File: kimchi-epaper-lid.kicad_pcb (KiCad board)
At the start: 4 copper layers, 65 x 32 mm, 8 parts, among them J1 DF40HC(3.5)-60DS, J2 DF40HC(3.5)-60DS, U1 24C32

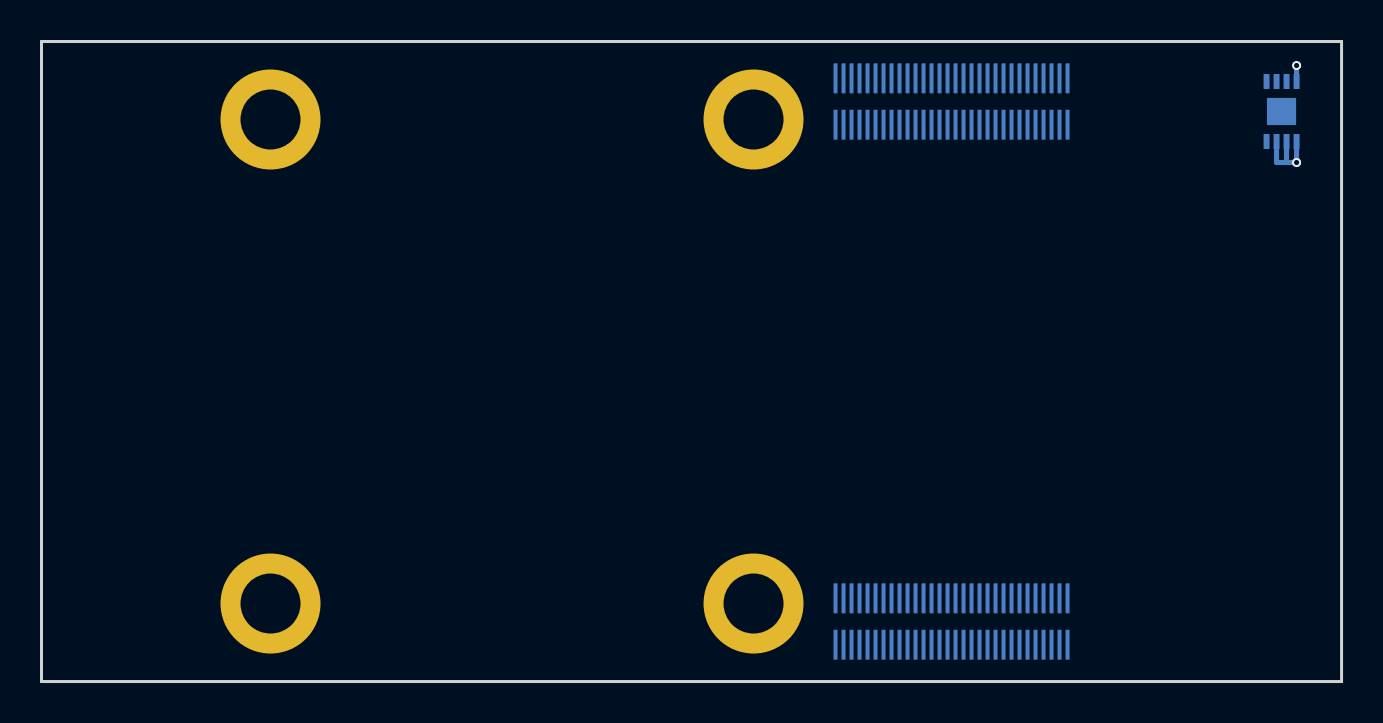
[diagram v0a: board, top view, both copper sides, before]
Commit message: prouting a few components and updated position
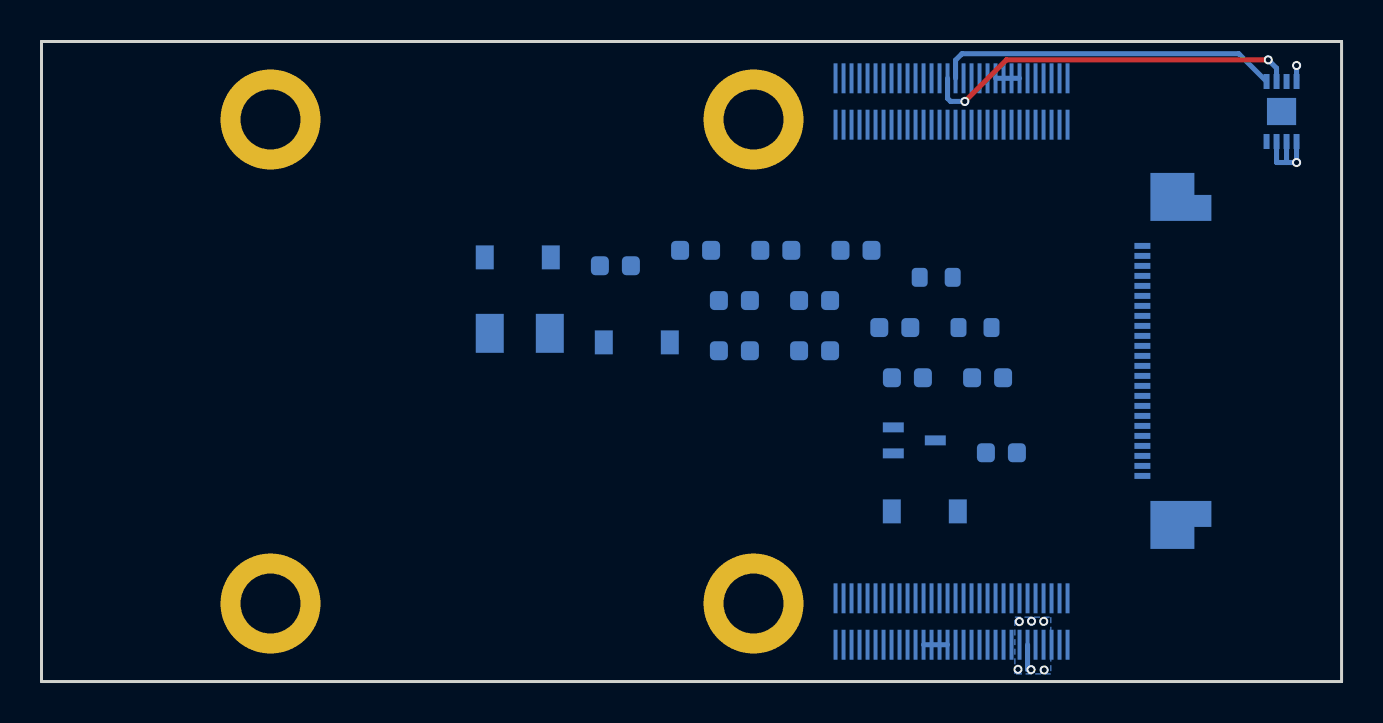
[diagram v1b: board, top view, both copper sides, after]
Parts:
- added C1: 2.2uF, Capacitor_SMD:C_0603_1608Metric, B.Cu at (154.3, 110.8)
- added C10: 1uF, Capacitor_SMD:C_0603_1608Metric, B.Cu at (149.7, 108.3)
- added C11: 1uF, Capacitor_SMD:C_0603_1608Metric, B.Cu at (141.6, 109.5)
- added C12: 0.1uF, Capacitor_SMD:C_0603_1608Metric, B.Cu at (147.7, 104.4)
- added C2: 1uF, Capacitor_SMD:C_0603_1608Metric, B.Cu at (135.7, 105.2)
- added C3: 1uF, Capacitor_SMD:C_0603_1608Metric, B.Cu at (145.7, 109.5)
- added C4: 1uF, Capacitor_SMD:C_0603_1608Metric, B.Cu at (141.6, 107.0)
- added C5: 1uF, Capacitor_SMD:C_0603_1608Metric, B.Cu at (139.7, 104.4)
- added C6: 1uF, Capacitor_SMD:C_0603_1608Metric, B.Cu at (150.3, 110.8)
- added C7: 1uF, Capacitor_SMD:C_0603_1608Metric, B.Cu at (143.7, 104.4)
- added C8: 1uF, Capacitor_SMD:C_0603_1608Metric, B.Cu at (145.7, 107.0)
- added C9: 1uF, Capacitor_SMD:C_0603_1608Metric, B.Cu at (155.0, 114.6)
- added D1: MBR0530T3G, Diode_SMD:D_SOD-123, B.Cu at (130.8, 104.8)
- added D2: MBR0530T3G, Diode_SMD:D_SOD-123, B.Cu at (136.8, 109.0)
- added D3: MBR0530T3G, Diode_SMD:D_SOD-123, B.Cu at (151.2, 117.5)
- added L1: 68uH, NLV32T-680J-EF:INDM3225X240N, B.Cu at (130.9, 108.6)
- added Q1: SI1308EDL-T1-BE3, SI1308EDL-T1-BE3:SOT65P210X110-3N, B.Cu at (150.6, 113.9)
- added R1: 10k, Resistor_SMD:R_0603_1608Metric, B.Cu at (153.7, 108.3)
- added R2: 2.2k, Resistor_SMD:R_0603_1608Metric, B.Cu at (151.7, 105.8)
- added X1: 52435-2471, epaper-fpc-connector:MOLEX_52435-2471, B.Cu at (162.0, 110.0)
- renumbered H3 to H2, H2 to H3
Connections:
- J1 pad 1: (no net) -> /USDHC3_CMD
- J1 pad 17: (no net) -> I2C3_SDA
- J1 pad 18: (no net) -> I2C3_SCL
- J1 pad 19: (no net) -> I2C2_SDA
- J1 pad 2: (no net) -> /USDHC3_CLK
- J1 pad 20: (no net) -> I2C2_SCL
- J1 pad 21: (no net) -> I2C1_SDA
- J1 pad 22: (no net) -> I2C1_SCL
- J1 pad 23: (no net) -> ECSPI1_SCLK
- J1 pad 24: (no net) -> ECSPI1_SS0
- J1 pad 25: (no net) -> ECSPI1_MOSI
- J1 pad 26: (no net) -> ECSPI1_MISO
- J1 pad 27: (no net) -> ECSPI2_SCLK
- J1 pad 28: (no net) -> ECSPI2_SS0
- J1 pad 29: (no net) -> ECSPI2_MOSI
- J1 pad 3: (no net) -> /USDHC3_DATA3
- J1 pad 30: (no net) -> ECSPI2_MISO
- J1 pad 31: (no net) -> /DISP_D0_N
- J1 pad 32: (no net) -> /DISP_D0_P
- J1 pad 33: (no net) -> /DISP_D1_N
- J1 pad 34: (no net) -> /DISP_D1_P
- J1 pad 35: (no net) -> /DISP_CK_N
- J1 pad 36: (no net) -> /DISP_CK_P
- J1 pad 37: (no net) -> /DISP_D2_N
- J1 pad 38: (no net) -> /DISP_D2_P
- J1 pad 39: (no net) -> /DISP_D3_N
- J1 pad 4: (no net) -> /USDHC3_DATA0
- J1 pad 40: (no net) -> /DISP_D3_P
- J1 pad 41: (no net) -> /CAM_D0_N
- J1 pad 42: (no net) -> /CAM_D0_P
- J1 pad 43: (no net) -> /CAM_D1_N
- J1 pad 44: (no net) -> /CAM_D1_P
- J1 pad 45: (no net) -> /CAM_CK_N
- J1 pad 46: (no net) -> /CAM_CK_P
- J1 pad 47: (no net) -> /CAM_D2_N
- J1 pad 48: (no net) -> /CAM_D2_P
- J1 pad 49: (no net) -> /CAM_D3_N
- J1 pad 5: (no net) -> /USDHC3_DATA1
- J1 pad 50: (no net) -> /CAM_D3_P
- J1 pad 52: (no net) -> UIM_VPP
- J1 pad 53: (no net) -> UIM_RESET_N
- J1 pad 54: (no net) -> UIM_CLK
- J1 pad 55: (no net) -> UIM_DATA
- J1 pad 56: (no net) -> UIM_PWR
- J1 pad 57: (no net) -> USB2_VBUS
- J1 pad 58: (no net) -> USB2_ID
- J1 pad 59: (no net) -> USB2_DN
- J1 pad 6: (no net) -> /USDHC3_DATA2
- J1 pad 60: (no net) -> USB2_DP
- J2 pad 1: (no net) -> /ENET_MDIO
- J2 pad 10: (no net) -> /ENET_TD0
- J2 pad 11: (no net) -> /ENET_TD3
- J2 pad 12: (no net) -> /ENET_TD2
- J2 pad 13: (no net) -> /ENET_TX_CTL
- J2 pad 14: (no net) -> /ENET_TXC
- J2 pad 15: (no net) -> SAI2_RXD0
- J2 pad 16: (no net) -> SAI2_TXFS
- J2 pad 17: (no net) -> SAI2_RXC
- J2 pad 18: (no net) -> SAI2_TXD0
- J2 pad 19: (no net) -> SAI2_TXC
- J2 pad 2: (no net) -> /ENET_MDC
- J2 pad 20: (no net) -> SAI2_MCLK
- J2 pad 21: (no net) -> SAI2_RXFS
- J2 pad 22: (no net) -> GPIO1[15]
- J2 pad 23: (no net) -> GPIO1[14]
- J2 pad 24: (no net) -> GPIO1[13]
- J2 pad 25: (no net) -> GPIO1[12]
- J2 pad 26: (no net) -> GPIO1[11]
- J2 pad 27: (no net) -> GPIO1[10]
- J2 pad 28: (no net) -> GPIO1[9]
- J2 pad 29: (no net) -> GPIO1[1]
- J2 pad 3: (no net) -> /ENET_RD3
- J2 pad 30: (no net) -> GPIO1[0]
- J2 pad 31: (no net) -> SAI3_TXC
- J2 pad 32: (no net) -> SAI3_TXD
- J2 pad 33: (no net) -> SAI3_RXD
- J2 pad 34: (no net) -> SAI3_RXFS
- J2 pad 35: (no net) -> SAI3_RXC
- J2 pad 36: (no net) -> SAI3_TXFS
- J2 pad 37: (no net) -> SAI3_MCLK
- J2 pad 4: (no net) -> /ENET_RD1
- J2 pad 46: (no net) -> UART1_TX
- J2 pad 47: (no net) -> UART1_RX
- J2 pad 48: (no net) -> UART3_TX
- J2 pad 49: (no net) -> UART3_RX
- J2 pad 5: (no net) -> /ENET_RD2
- J2 pad 58: (no net) -> Net-(J2-Pad58)
- J2 pad 59: (no net) -> PCIE_USB_D_P
- J2 pad 6: (no net) -> /ENET_RD0
- J2 pad 60: (no net) -> PCIE_USB_D_N
- J2 pad 7: (no net) -> /ENET_RXC
- J2 pad 8: (no net) -> /ENET_RX_CTL
- J2 pad 9: (no net) -> /ENET_TD1
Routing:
- net I2C4_SCL: track 0.00 -> 19.2 mm, vias 0 -> 2
- net I2C4_SDA: track 0.00 -> 17.2 mm
- net VDD_3V3: track 4.95 -> 6.20 mm, vias 2 -> 8
- net VDD_5V: track 0.00 -> 1.20 mm
- net VDD_1V8: track 0.00 -> 1.20 mm
- added copper zone on B.Cu, net VDD_3V3

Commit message: Completed routing
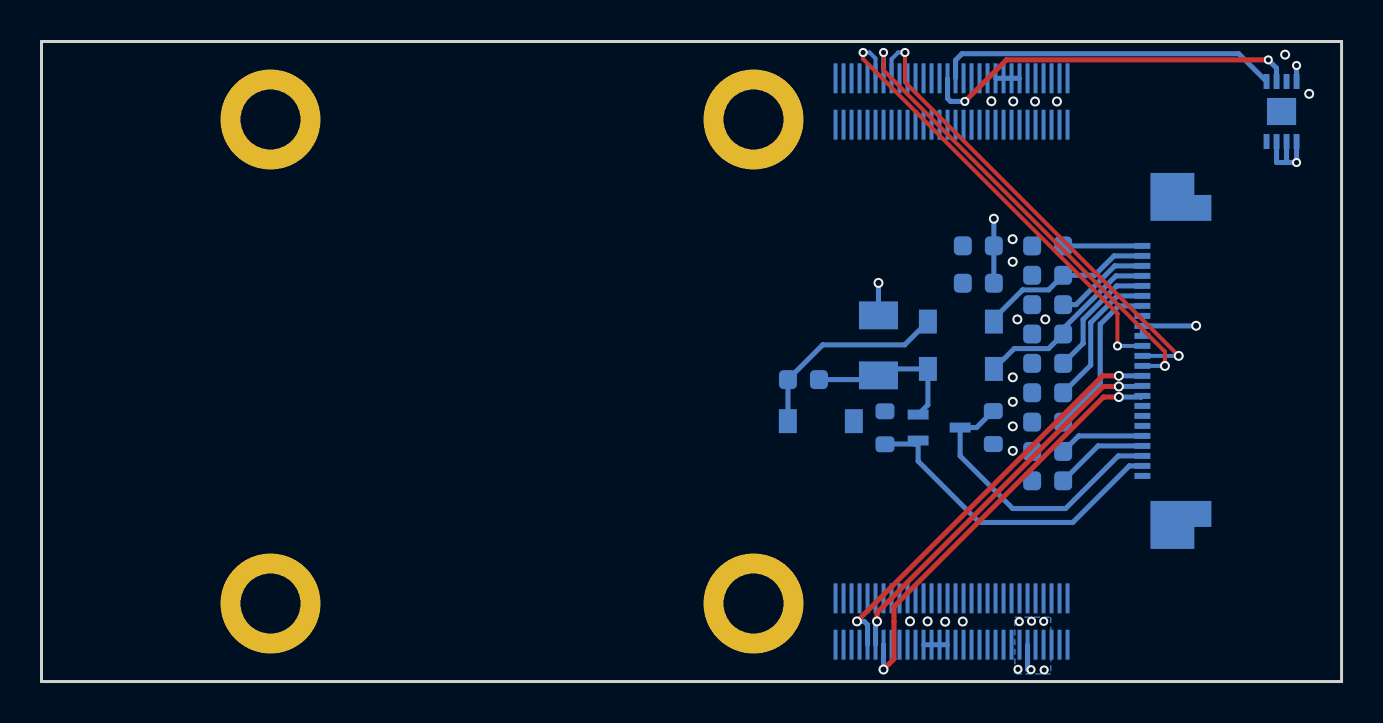
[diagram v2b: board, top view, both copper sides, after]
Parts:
- moved C5 19.6 mm to (157.3, 113.0)
- moved L1 17.9 mm to (148.8, 109.2), turned to 270 degrees
- moved D1 17.2 mm to (146.0, 113.0), turned to 180 degrees
- moved C11 16.5 mm to (157.3, 114.5)
- moved D2 16.2 mm to (153.0, 108.0)
- moved C4 15.7 mm to (157.3, 105.7)
- moved C7 14.7 mm to (157.3, 110.1), turned to 180 degrees
- moved C3 11.7 mm to (157.3, 108.6), turned to 180 degrees
- moved C8 11.7 mm to (157.3, 107.2), turned to 180 degrees
- moved C2 11.0 mm to (145.1, 110.9)
- moved C10 10.8 mm to (157.3, 116.0), turned to 180 degrees
- moved C9 10.6 mm to (157.3, 104.2)
- moved R2 8.03 mm to (154.6, 113.3), turned to 270 degrees
- moved D3 7.35 mm to (153.0, 110.4), turned to 180 degrees
- moved C6 7.05 mm to (157.3, 111.6), turned to 180 degrees
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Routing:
- net ECSPI1_SCLK: track 0.00 -> 24.4 mm, vias 0 -> 2
- net ECSPI1_SS0: track 0.00 -> 23.9 mm, vias 0 -> 2
- net ECSPI1_MOSI: track 0.00 -> 22.9 mm, vias 0 -> 2
- net SAI3_MCLK: track 0.00 -> 21.4 mm, vias 0 -> 2
- net SAI3_RXC: track 0.00 -> 20.9 mm, vias 0 -> 2
- net SAI3_TXFS: track 0.00 -> 19.6 mm, vias 0 -> 2
- net GDR: track 0.00 -> 16.4 mm
- net RESE: track 0.00 -> 14.7 mm
- net Net-(C2-Pad1): track 0.00 -> 10.3 mm
- net PREVGH: track 0.00 -> 9.51 mm
- net PREVGL: track 0.00 -> 8.87 mm
- net Net-(C2-Pad2): track 0.00 -> 8.15 mm
- net Net-(C5-Pad2): track 0.00 -> 8.15 mm
- net VDD_3V3: track 6.20 -> 14.2 mm, vias 8 -> 11
- net Net-(C6-Pad1): track 0.00 -> 7.21 mm
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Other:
- board text added: "1"
- board text added: "24"

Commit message: Updated routing
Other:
- rule solder_mask_min_width: 0.1016 -> 0.001

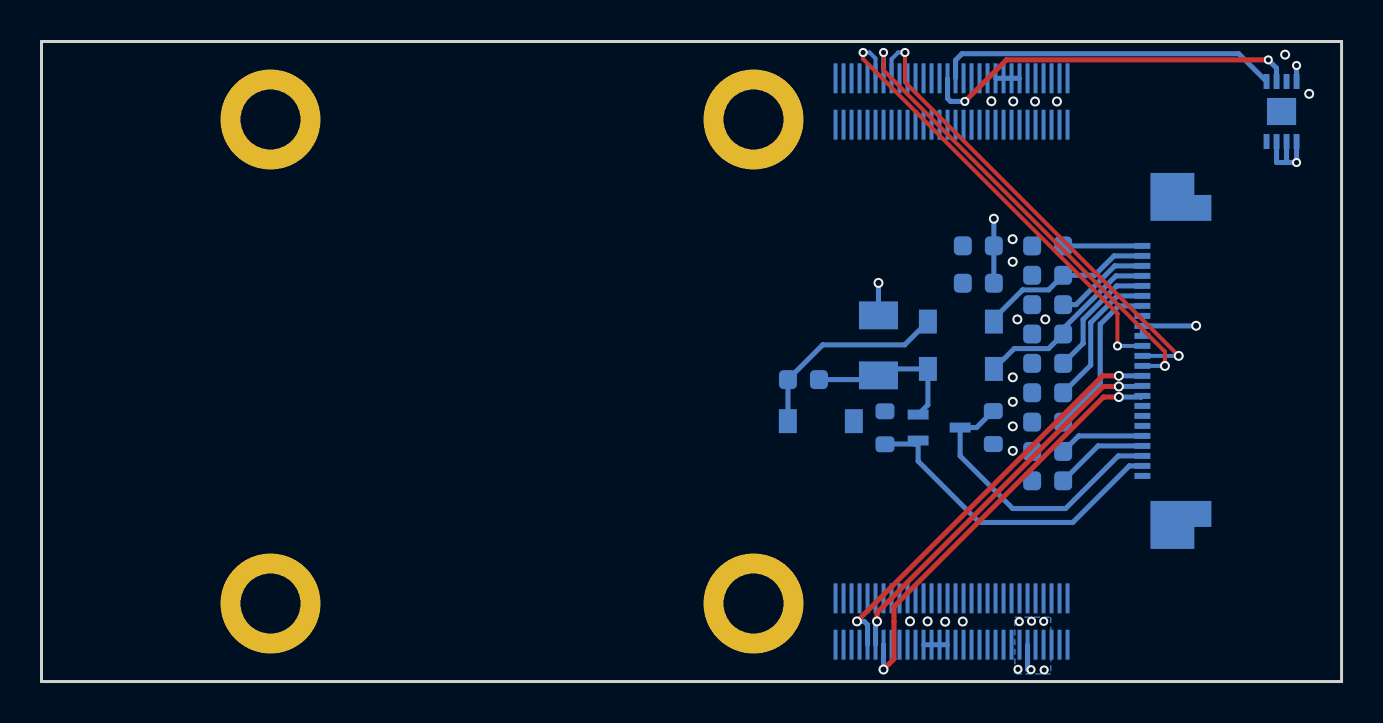
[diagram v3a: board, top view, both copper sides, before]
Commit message: Fixed issues with routing
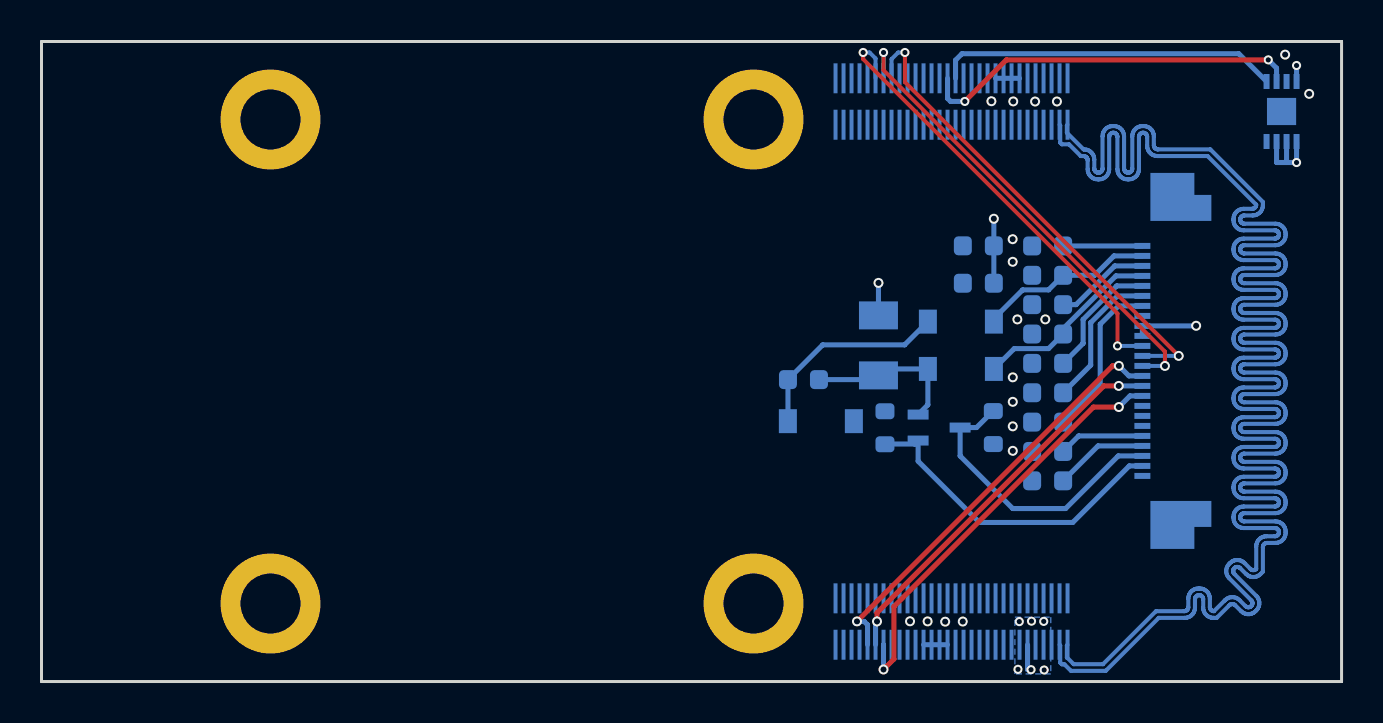
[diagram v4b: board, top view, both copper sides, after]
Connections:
- J1 pad 59: USB2_DN -> PCIE_USB_D_N
- J1 pad 60: USB2_DP -> PCIE_USB_D_P
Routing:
- net PCIE_USB_D_P: track 0.00 -> 99.4 mm
- net PCIE_USB_D_N: track 0.00 -> 98.5 mm
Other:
- rule pad_to_mask_clearance: 0.0508 -> 0
